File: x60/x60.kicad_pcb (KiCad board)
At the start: 2 copper layers, 150 parts, among them SW1 SW_Push, U1 ATmega32U4-AU, Y1 16mhz

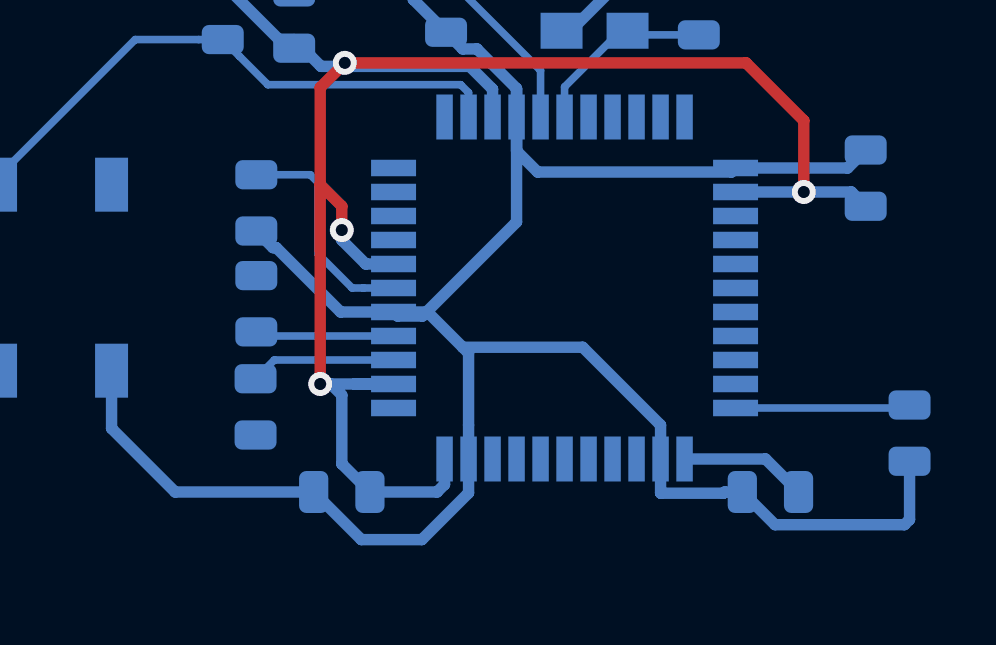
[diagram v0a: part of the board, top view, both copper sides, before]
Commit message: fixed mcu routing
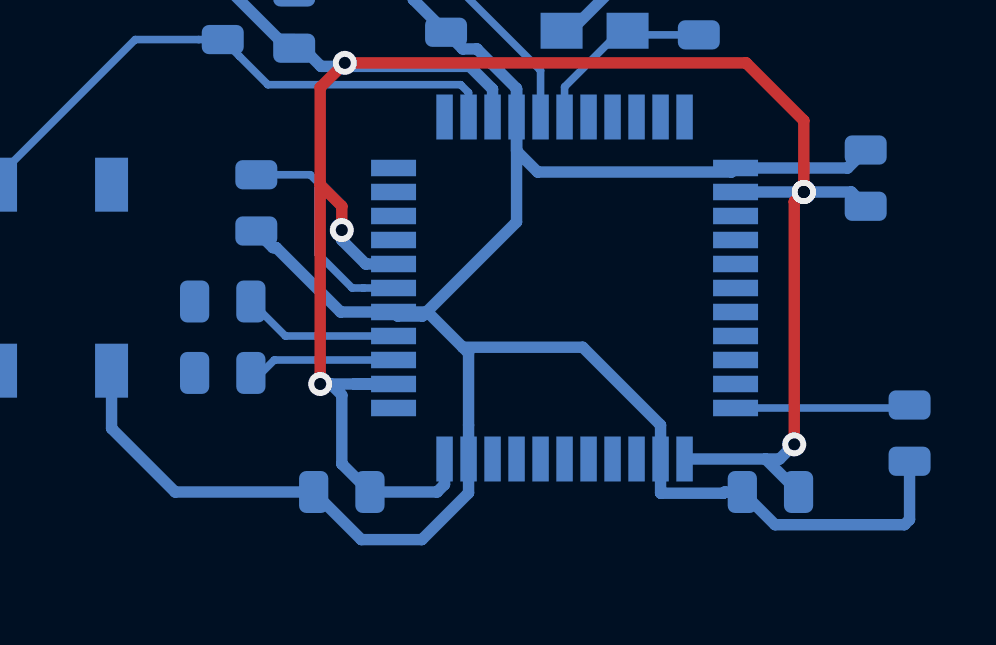
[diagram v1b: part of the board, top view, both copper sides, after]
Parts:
- moved R1 1.57 mm to (97.6, 87.3), turned to 180 degrees
- moved R2 1.12 mm to (97.6, 84.9), turned to 180 degrees
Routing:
- net +5V: track 65.3 -> 75.0 mm, vias 4 -> 6
- net Net-(R2-Pad1): track 4.63 -> 5.23 mm
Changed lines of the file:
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@@
     (thickness 1.6)
     (drawings 1)
-    (tracks 127)
+    (tracks 133)
     (zones 0)
     (modules 150)
@@
   )
   (module Resistor_SMD:R_0805_2012Metric (layer B.Cu)
-    (at 98.75 85.00625 90)
+    (at 97.63125 84.93125 180)
     (descr "Resistor SMD 0805 (2012 Metric), square (rectangular) end terminal, IPC_7351 nominal, (Body size source: https://docs.google.com/spreadsheets/d/1BsfQQcO9C6DZCsRaXUlFlo91Tg2WpOkGARC1WS5S8t0/edit?usp=sharing), generated with kicad-footprint-generator")
     (tags resistor)
     (attr smd)
-    (fp_text reference R2 (at 0 1.65 90) (layer B.SilkS)
+    (fp_text reference R2 (at 0 1.65) (layer B.SilkS)
       (effects (font (size 1 1) (thickness 0.15)) (justify mirror))
     )
-    (fp_text value 22k (at 0 -1.65 90) (layer B.Fab)
+    (fp_text value 22k (at 0 -1.65) (layer B.Fab)
       (effects (font (size 1 1) (thickness 0.15)) (justify mirror))
     )
-    (fp_text user %R (at 0 0 90) (layer B.Fab)
+    (fp_text user %R (at 0 0) (layer B.Fab)
       (effects (font (size 0.5 0.5) (thickness 0.08)) (justify mirror))
     )
@@
     (fp_line (start -1 0.6) (end 1 0.6) (layer B.Fab) (width 0.1))
     (fp_line (start -1 -0.6) (end -1 0.6) (layer B.Fab) (width 0.1))
-    (pad 2 smd roundrect (at 0.9375 0 90) (size 0.975 1.4) (layers B.Cu B.Paste B.Mask) (roundrect_rratio 0.25)
+    (pad 2 smd roundrect (at 0.9375 0 180) (size 0.975 1.4) (layers B.Cu B.Paste B.Mask) (roundrect_rratio 0.25)
       (net 88 D+))
-    (pad 1 smd roundrect (at -0.9375 0 90) (size 0.975 1.4) (layers B.Cu B.Paste B.Mask) (roundrect_rratio 0.25)
+    (pad 1 smd roundrect (at -0.9375 0 180) (size 0.975 1.4) (layers B.Cu B.Paste B.Mask) (roundrect_rratio 0.25)
       (net 89 "Net-(R2-Pad1)"))
     (model ${KISYS3DMOD}/Resistor_SMD.3dshapes/R_0805_2012Metric.wrl
@@
   )
   (module Resistor_SMD:R_0805_2012Metric (layer B.Cu)
-    (at 98.725 88.44375 270)
+    (at 97.63125 87.3125 180)
     (descr "Resistor SMD 0805 (2012 Metric), square (rectangular) end terminal, IPC_7351 nominal, (Body size source: https://docs.google.com/spreadsheets/d/1BsfQQcO9C6DZCsRaXUlFlo91Tg2WpOkGARC1WS5S8t0/edit?usp=sharing), generated with kicad-footprint-generator")
     (tags resistor)
     (attr smd)
-    (fp_text reference R1 (at 0 1.65 270) (layer B.SilkS)
+    (fp_text reference R1 (at 0 1.65 180) (layer B.SilkS)
       (effects (font (size 1 1) (thickness 0.15)) (justify mirror))
     )
-    (fp_text value 22k (at 0 -1.65 270) (layer B.Fab)
+    (fp_text value 22k (at 0 -1.65 180) (layer B.Fab)
       (effects (font (size 1 1) (thickness 0.15)) (justify mirror))
     )
-    (fp_text user %R (at 0 0 270) (layer B.Fab)
+    (fp_text user %R (at 0 0 180) (layer B.Fab)
       (effects (font (size 0.5 0.5) (thickness 0.08)) (justify mirror))
     )
@@
     (fp_line (start -1 0.6) (end 1 0.6) (layer B.Fab) (width 0.1))
     (fp_line (start -1 -0.6) (end -1 0.6) (layer B.Fab) (width 0.1))
-    (pad 2 smd roundrect (at 0.9375 0 270) (size 0.975 1.4) (layers B.Cu B.Paste B.Mask) (roundrect_rratio 0.25)
+    (pad 2 smd roundrect (at 0.9375 0 180) (size 0.975 1.4) (layers B.Cu B.Paste B.Mask) (roundrect_rratio 0.25)
       (net 86 D-))
-    (pad 1 smd roundrect (at -0.9375 0 270) (size 0.975 1.4) (layers B.Cu B.Paste B.Mask) (roundrect_rratio 0.25)
+    (pad 1 smd roundrect (at -0.9375 0 180) (size 0.975 1.4) (layers B.Cu B.Paste B.Mask) (roundrect_rratio 0.25)
       (net 87 "Net-(R1-Pad1)"))
     (model ${KISYS3DMOD}/Resistor_SMD.3dshapes/R_0805_2012Metric.wrl
@@
   (segment (start 117 81.28125) (end 117 78.9) (width 0.381) (layer F.Cu) (net 2))
   (segment (start 117 78.9) (end 115.077249 76.977249) (width 0.381) (layer F.Cu) (net 2))
+  (via (at 116.68125 89.69375) (size 0.8) (drill 0.4) (layers F.Cu B.Cu) (net 2))
+  (segment (start 115.725 90.18125) (end 116.19375 90.18125) (width 0.381) (layer B.Cu) (net 2))
+  (segment (start 116.19375 90.18125) (end 116.68125 89.69375) (width 0.381) (layer B.Cu) (net 2))
+  (via (at 117 81.28125) (size 0.8) (drill 0.4) (layers F.Cu B.Cu) (net 2))
+  (segment (start 116.68125 89.69375) (end 116.68125 81.6) (width 0.381) (layer F.Cu) (net 2))
+  (segment (start 116.68125 81.6) (end 117 81.28125) (width 0.381) (layer F.Cu) (net 2))
   (segment (start 111.2625 76.04375) (end 111.125 75.90625) (width 0.254) (layer B.Cu) (net 3))
   (segment (start 113.5 76.04375) (end 111.2625 76.04375) (width 0.254) (layer B.Cu) (net 3))
@@
   (segment (start 99.35 86.88125) (end 98.725 87.50625) (width 0.254) (layer B.Cu) (net 87))
   (segment (start 103.325 86.88125) (end 99.35 86.88125) (width 0.254) (layer B.Cu) (net 87))
-  (segment (start 98.8875 86.08125) (end 98.75 85.94375) (width 0.254) (layer B.Cu) (net 89))
-  (segment (start 103.325 86.08125) (end 98.8875 86.08125) (width 0.254) (layer B.Cu) (net 89))
+  (segment (start 99.71875 86.08125) (end 98.56875 84.93125) (width 0.254) (layer B.Cu) (net 89))
+  (segment (start 103.325 86.08125) (end 99.71875 86.08125) (width 0.254) (layer B.Cu) (net 89))
   (segment (start 98.187487 76.756237) (end 97.63125 76.2) (width 0.254) (layer B.Cu) (net 90))
   (segment (start 99.135499 77.704249) (end 98.187487 76.756237) (width 0.254) (layer B.Cu) (net 90))

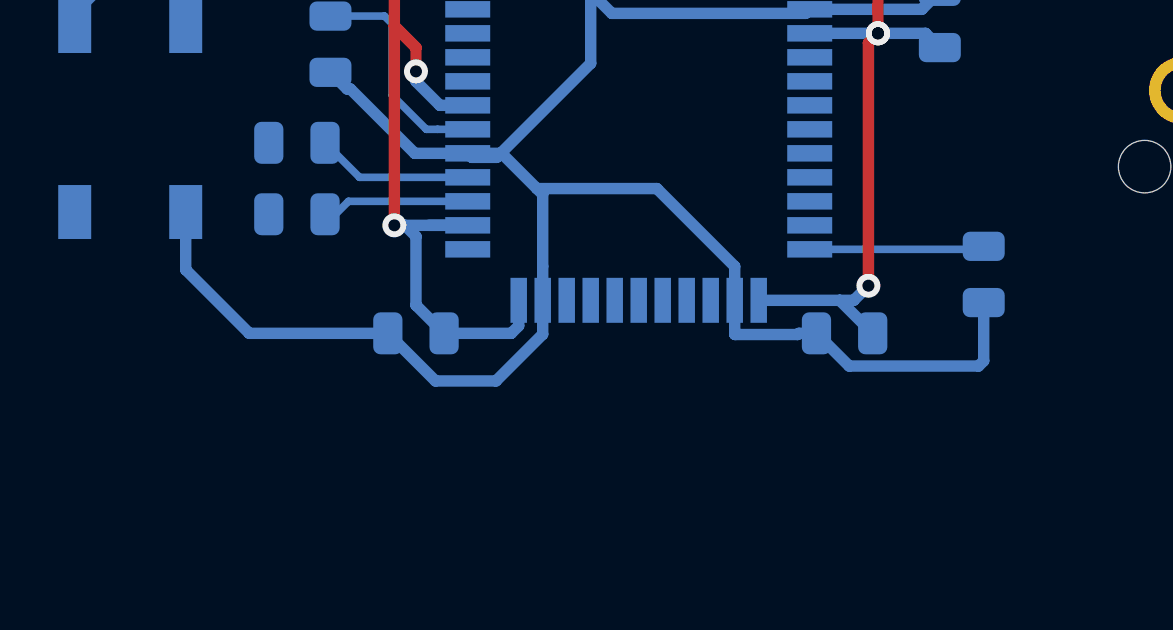
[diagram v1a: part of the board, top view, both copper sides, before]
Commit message: fixed capcitors being placed too close to the pcb
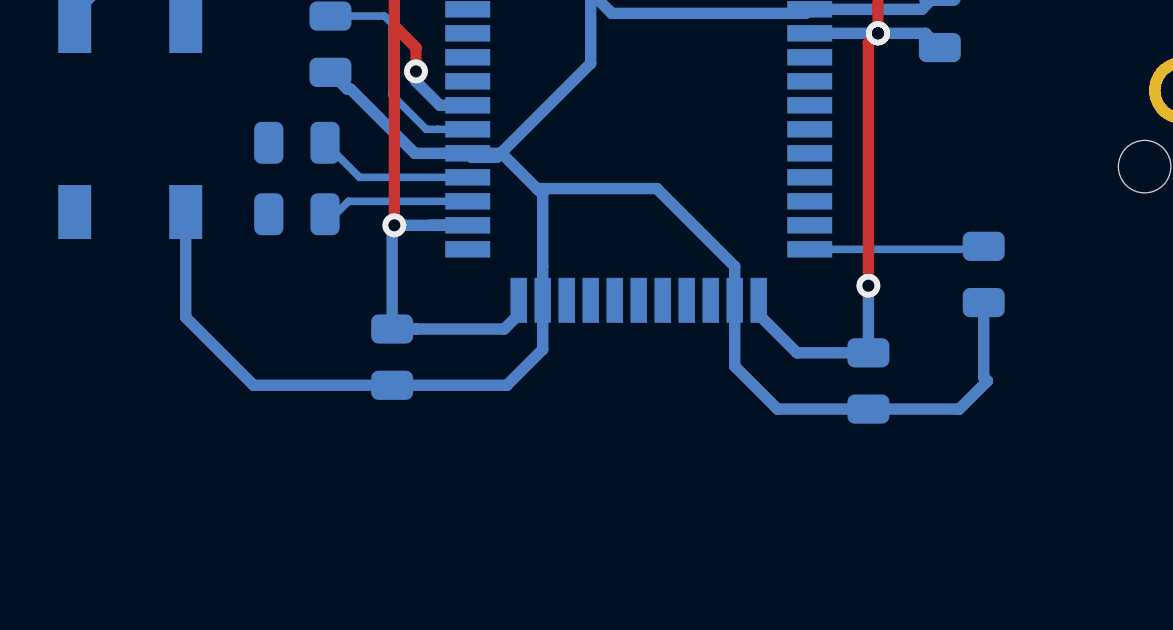
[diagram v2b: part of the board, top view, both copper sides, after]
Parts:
- moved C4 1.77 mm to (116.7, 92.9), turned to 270 degrees
- moved C7 1.12 mm to (100.8, 92.1), turned to 270 degrees
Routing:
- net GND: track 101.8 -> 105.3 mm
- net +5V: track 75.0 -> 77.3 mm

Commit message: wired all rows and columns
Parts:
- MX40: moved to F.Cu
- moved MX71 90.0 mm to (258.1, 169.9)
- moved MX40 89.7 mm to (216.7, 150.9)
- moved C6 89.7 mm to (150.0, 165.0)
- moved MX36 89.7 mm to (173.8, 169.9)
- moved MX59 89.7 mm to (302.4, 169.9)
- moved MX69 89.7 mm to (161.9, 169.9)
- moved MX70 89.7 mm to (233.4, 169.9)
- moved MX72 89.7 mm to (281.0, 169.9)
- moved MX73 89.7 mm to (304.8, 169.9)
- moved C2 89.7 mm to (144.5, 159.2)
- moved C5 89.7 mm to (129.7, 165.8)
- moved D48 89.7 mm to (264.3, 150.8)
- moved D53 89.7 mm to (269.9, 150.8)
- moved MX14 89.7 mm to (69.1, 169.9)
- moved MX22 89.7 mm to (140.5, 150.8)
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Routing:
- net ROW3: track 0.00 -> 344.1 mm
- net ROW2: track 0.00 -> 289.3 mm
- net ROW4: track 0.00 -> 266.7 mm
- net ROW1: track 0.00 -> 254.0 mm
- net ROW5: track 0.00 -> 193.9 mm
- net COL3: track 0.00 -> 144.9 mm
- net COL5: track 0.00 -> 144.6 mm
- net COL8: track 0.00 -> 125.1 mm
- net COL12: track 0.00 -> 120.0 mm
- net COL13: track 0.00 -> 114.6 mm
- net COL1: track 0.00 -> 108.2 mm
- net COL11: track 0.00 -> 107.5 mm
- net COL14: track 0.00 -> 104.6 mm
- net COL2: track 0.00 -> 103.5 mm
- net COL4: track 0.00 -> 93.4 mm
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
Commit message: connected rows to mcu
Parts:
- moved C1 3.48 mm to (134.3, 158.8)
- moved C3 3.48 mm to (139.4, 158.3)
- moved C4 3.48 mm to (151.0, 176.1)
- moved C7 3.48 mm to (135.1, 175.3)
- moved R4 3.48 mm to (154.8, 172.6)
- moved U1 3.48 mm to (143.3, 167.7)
- moved Y1 3.48 mm to (144.3, 158.3)
- moved SW1 3.48 mm to (126.4, 167.4)
- moved C2 3.48 mm to (147.8, 158.4)
- moved C5 3.48 mm to (133.1, 164.9)
- moved C6 3.48 mm to (153.4, 164.1)
- moved R1 3.48 mm to (132.0, 170.6)
- moved R2 3.48 mm to (132.0, 168.2)
- moved R3 3.48 mm to (132.0, 158.5)
- moved MX36 0.08 mm to (173.9, 169.9)
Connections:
- U1 pad 38: Net-(U1-Pad38) -> ROW1
- U1 pad 39: Net-(U1-Pad39) -> ROW2
- U1 pad 40: Net-(U1-Pad40) -> ROW3
- U1 pad 41: Net-(U1-Pad41) -> ROW4
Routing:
- net ROW1: track 254.0 -> 462.7 mm
- net ROW2: track 289.3 -> 484.1 mm
- net ROW3: track 344.1 -> 520.5 mm
- net ROW4: track 266.7 -> 431.7 mm

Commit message: wired all rows and columns to mcu
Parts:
- moved R4 2.47 mm to (153.3, 174.5)
- moved MX69 0.08 mm to (161.9, 169.9)
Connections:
- U1 pad 10: Net-(U1-Pad10) -> COL1
- U1 pad 11: Net-(U1-Pad11) -> COL2
- U1 pad 18: Net-(U1-Pad18) -> COL4
- U1 pad 19: Net-(U1-Pad19) -> COL5
- U1 pad 22: Net-(U1-Pad22) -> COL6
- U1 pad 25: Net-(U1-Pad25) -> COL7
- U1 pad 26: Net-(U1-Pad26) -> COL8
- U1 pad 27: Net-(U1-Pad27) -> COL9
- U1 pad 28: Net-(U1-Pad28) -> COL10
- U1 pad 29: Net-(U1-Pad29) -> COL11
- U1 pad 30: Net-(U1-Pad30) -> COL12
- U1 pad 31: Net-(U1-Pad31) -> COL13
- U1 pad 32: Net-(U1-Pad32) -> COL14
- U1 pad 36: Net-(U1-Pad36) -> ROW5
- U1 pad 37: Net-(U1-Pad37) -> COL3
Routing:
- net COL14: track 104.6 -> 266.7 mm, vias 0 -> 1
- net COL13: track 114.6 -> 266.1 mm, vias 0 -> 1
- net COL12: track 120.0 -> 245.7 mm, vias 0 -> 1
- net COL10: track 83.4 -> 193.4 mm, vias 0 -> 1
- net COL1: track 108.2 -> 206.9 mm, vias 0 -> 1
- net COL3: track 144.9 -> 242.7 mm, vias 0 -> 1
- net COL11: track 107.5 -> 197.1 mm, vias 0 -> 1
- net ROW5: track 193.9 -> 283.3 mm, vias 0 -> 2
- net COL9: track 82.4 -> 165.4 mm, vias 0 -> 1
- net COL2: track 103.5 -> 171.2 mm, vias 0 -> 1
- net COL4: track 93.4 -> 141.0 mm, vias 0 -> 1
- net +5V: track 77.3 -> 114.9 mm, vias 6 -> 5
- net COL7: track 79.2 -> 116.7 mm, vias 0 -> 1
- net COL5: track 144.6 -> 176.8 mm, vias 0 -> 1
- net COL6: track 85.6 -> 105.7 mm, vias 0 -> 1
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
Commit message: flipped spacebar stabs
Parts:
- MX36: footprint MX_Only:MXOnly-7U-NoLED -> MX_Only:MXOnly-7U-ReversedStabilizers-NoLED
- MX69: footprint MX_Only:MXOnly-6.25U-NoLED -> MX_Only:MXOnly-6.25U-ReversedStabilizers-NoLED
- moved D51 45.8 mm to (305.8, 138.6)
- moved D54 45.8 mm to (305.8, 194.2)
- moved MX57 45.8 mm to (333.6, 156.8)
- moved D61 45.8 mm to (353.4, 118.7)
- moved MX64 45.8 mm to (345.5, 118.7)
- moved D62 45.8 mm to (353.4, 175.9)
- moved MX50 45.8 mm to (297.9, 137.8)
- moved MX62 45.8 mm to (345.5, 175.9)
- moved C5 45.8 mm to (171.4, 190.0)
- moved D18 45.8 mm to (167.7, 176.7)
- moved D25 45.8 mm to (191.5, 138.6)
- moved D27 45.8 mm to (205.8, 176.7)
- moved D30 45.8 mm to (215.3, 156.8)
- moved D31 45.8 mm to (225.6, 176.7)
- moved D33 45.8 mm to (229.6, 138.6)
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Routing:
- net COL13: track 266.1 -> 262.9 mm
- net COL14: track 266.7 -> 263.6 mm
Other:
- board outline added: 0.1 x 0.5 mm
